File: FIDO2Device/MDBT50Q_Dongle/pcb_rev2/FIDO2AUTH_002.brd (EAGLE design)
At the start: 22.9 x 38.7 mm, 33 parts, among them CN1 TE-1734028, CN2 IF_5PIN_H, CN3 IF_3PIN, SW1 SKRPACE010, SW2 SKTADAE010, U1 MDBT50Q-P1M, U2 XC6206P332MR-G, X1 NX3215SA-32.768K

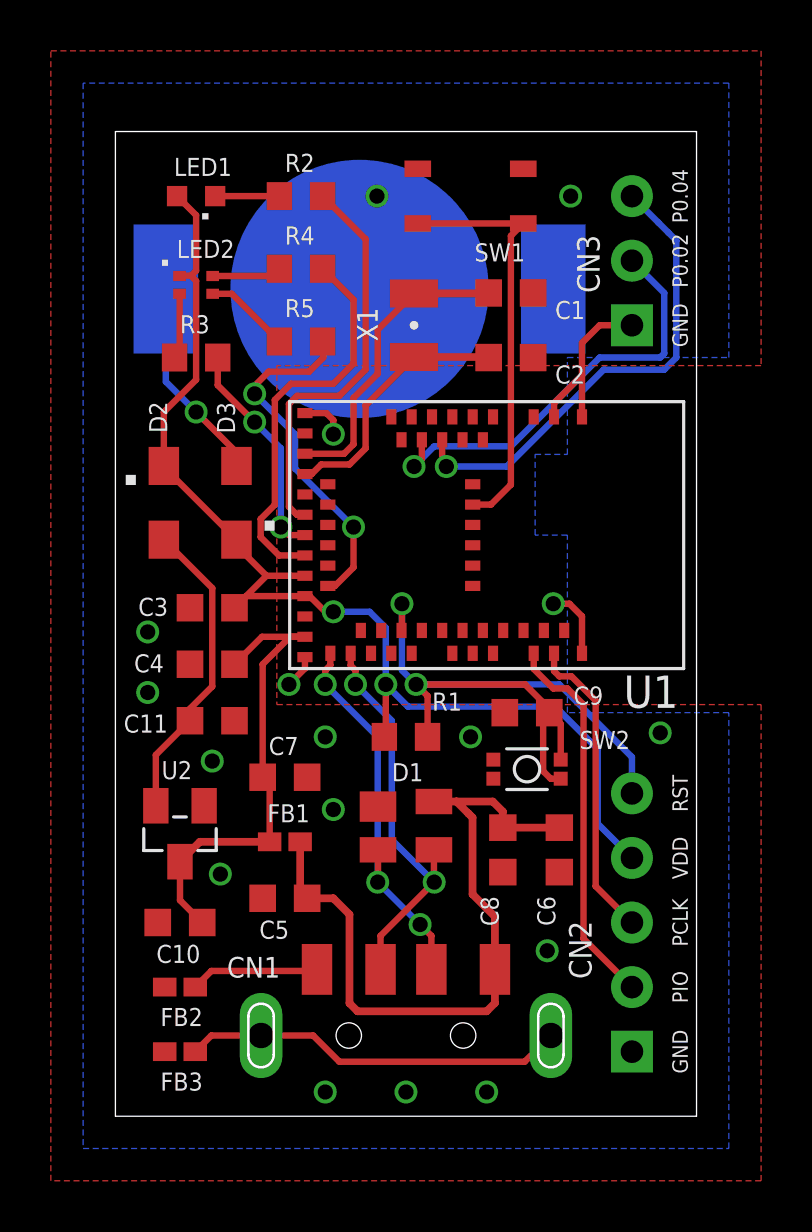
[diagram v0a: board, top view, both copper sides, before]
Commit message: 回路図・部品表を修正
・増えた部品は２点（LED3、R6）
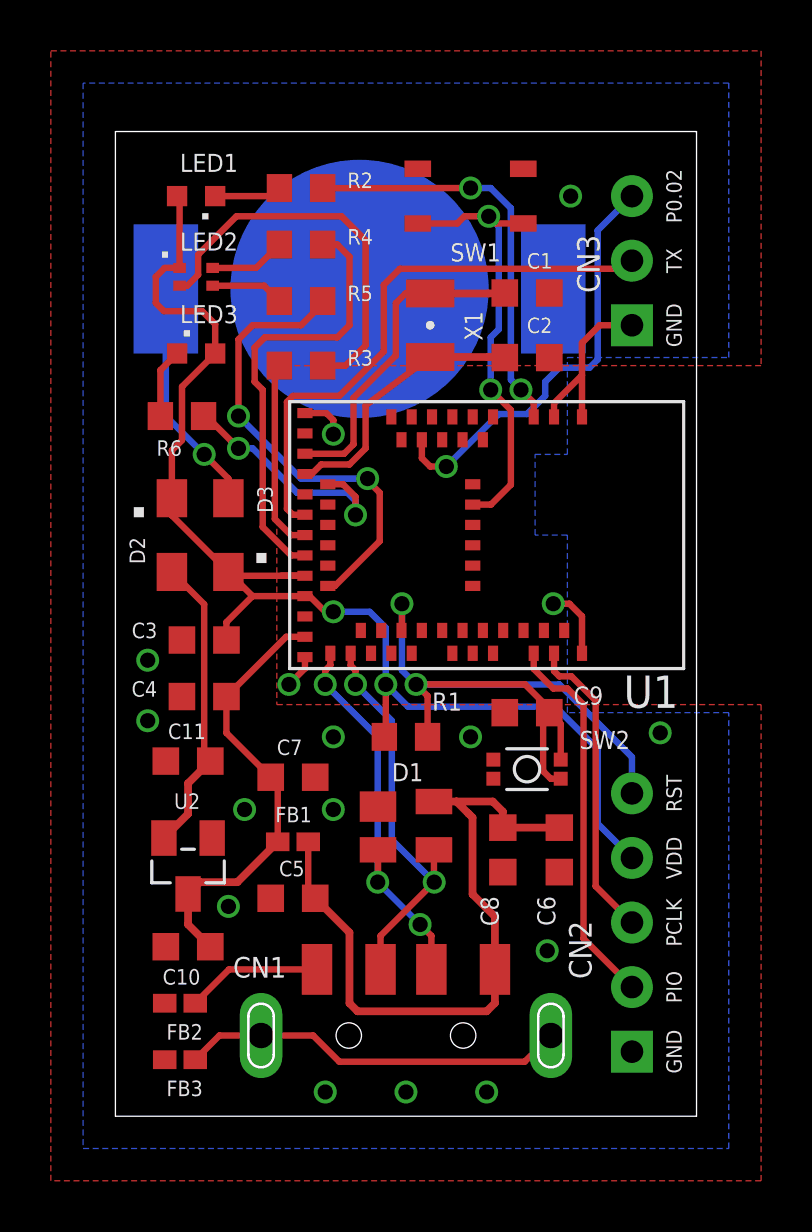
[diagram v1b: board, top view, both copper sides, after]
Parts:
- added LED3: APTD1608LSYCK, Parts:CHIPLED_0603
- added R6: 1.5k, Parts:R0603
- U1: device Parts:MDBT50Q-P1M -> Modules:MDBT50Q-P1M
- moved R3 4.14 mm to (7.30, 29.5), turned to 0 degrees
- moved C11 1.85 mm to (2.86, 14.0), turned to 180 degrees
- moved R5 1.59 mm to (7.30, 32.1)
- moved U2 1.31 mm to (2.86, 9.84)
- moved C3 1.31 mm to (3.49, 18.7)
- moved C4 1.31 mm to (3.49, 16.5)
- moved D2 1.31 mm to (2.22, 22.9)
- moved D3 1.31 mm to (4.45, 22.9)
- moved C10 1.00 mm to (2.86, 6.67)
- moved R4 0.95 mm to (7.30, 34.3)
- moved C1 0.63 mm to (16.2, 32.4)
- moved C2 0.63 mm to (16.2, 29.8)
- moved FB2 0.63 mm to (2.54, 4.45)
- moved X1 0.63 mm to (12.4, 31.1)
- moved LED2 0.32 mm to (3.17, 33.0)
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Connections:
- removed net AIN1: CN3.3, U1.9
- new net LED3: R6.1, U1.19
- new net N$8: LED3.C, R6.2
- new net UART_TX: CN3.2, U1.22
- net AIN0: now also CN3.3; no longer CN3.2
- net LED1: now also U1.3; no longer U1.22
- net VDD_NRF: now also LED3.A
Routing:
- net UART_TX: track 0.00 -> 22.4 mm
- net AIN1: track 19.0 -> 0.00 mm, vias 1 -> 0
- net N$1: track 2.59 -> 15.5 mm
- net LED3: track 0.00 -> 9.92 mm, vias 0 -> 2
- net VDD_NRF: track 45.9 -> 50.8 mm
- net LED2_B: track 13.9 -> 18.5 mm
- net N$8: track 0.00 -> 2.73 mm
- net LED2_G: track 15.6 -> 17.4 mm
- net VBUS_NRF: track 19.0 -> 17.4 mm
- net N$5: track 8.11 -> 9.25 mm
- net SW1: track 16.5 -> 17.4 mm, vias 0 -> 2
- net LED2_R: track 8.77 -> 7.84 mm, vias 2 -> 0
- net XL1: track 11.9 -> 12.8 mm
- net VBUS: track 28.1 -> 27.4 mm
- net N$6: track 2.75 -> 3.35 mm
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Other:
- board text added: "TX"
- board text removed: "P0.04"

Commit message: 基板の配線を修正
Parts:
- moved BAT1 0.16 mm to (9.45, 32.5)
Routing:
- net LED1: track 16.3 -> 32.9 mm
- net SW1: track 17.4 -> 29.2 mm
- net AIN0: track 16.8 -> 22.3 mm
- net 0V: track 13.2 -> 12.4 mm, vias 16 -> 18
